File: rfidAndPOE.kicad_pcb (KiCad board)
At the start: 4 copper layers, 100 x 50 mm, 126 parts, among them J1 0813-1X1T-57-F, J2 SWD, J3 MCU Port B, J4 MCU Port C, P1 PoE-, P2 PoE+, P3 GND, P4 +5V, P5 +12V, P6 +3V3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

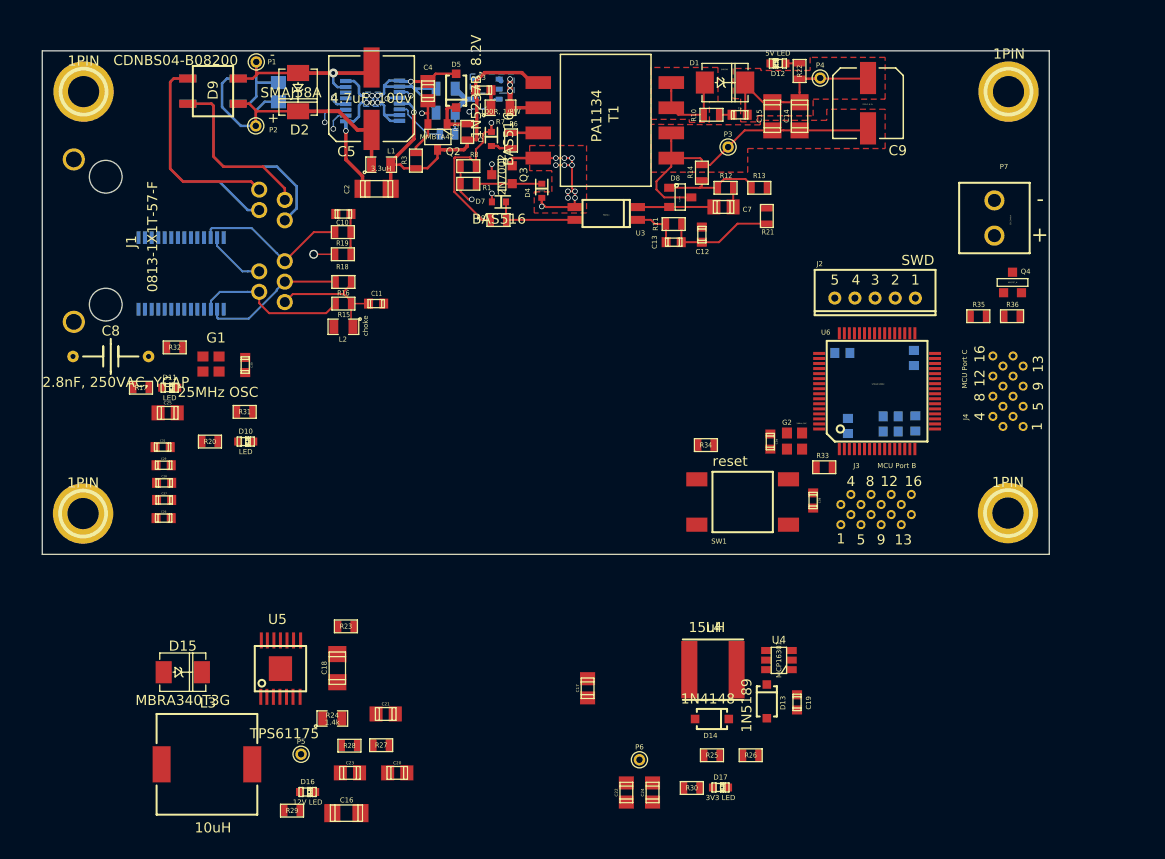
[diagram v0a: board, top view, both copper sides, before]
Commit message: Placed and routed most of the enc28j60 components. Moved TPS61175 (12v boost supply) and components in to good orientation. Almost ready to route. Added ground plane on most of the board.
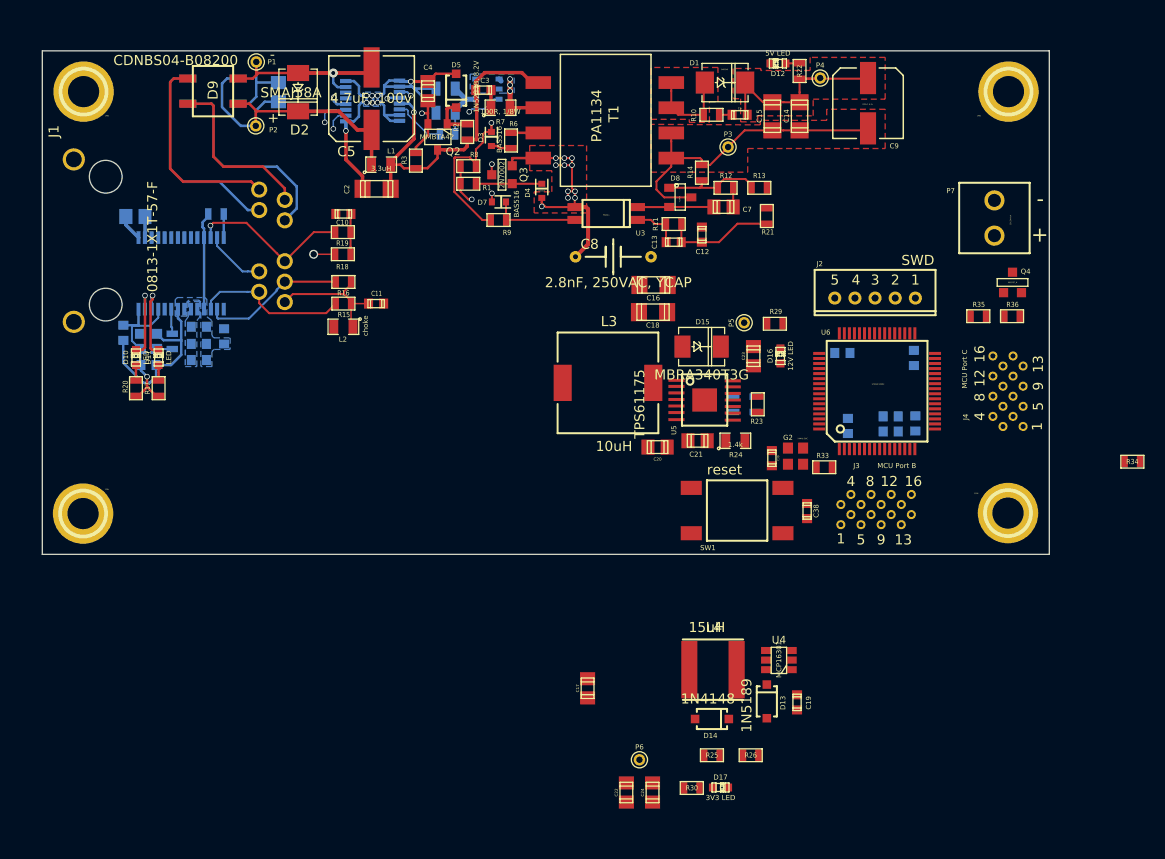
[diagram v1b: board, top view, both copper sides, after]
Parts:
- C25, C26, C27, C28, C29, C30, C31, G1, R27, R28, R31, R32: moved to B.Cu
- moved R29 68.1 mm to (150.6, 57.8)
- moved D16 63.9 mm to (151.1, 61.0), turned to 90 degrees
- moved P5 61.4 mm to (147.5, 57.7), turned to 90 degrees
- moved D15 60.8 mm to (143.3, 60.1)
- moved C16 60.7 mm to (138.5, 54.0), turned to 180 degrees
- moved C23 57.6 mm to (148.4, 61.0), turned to 90 degrees
- moved L3 55.0 mm to (134.0, 63.7)
- moved R28 52.7 mm to (148.6, 65.8), turned to 90 degrees
- moved C8 50.9 mm to (134.5, 51.1)
- moved U5 49.9 mm to (143.6, 65.4), turned to 270 degrees
- moved R27 48.7 mm to (146.4, 65.8), turned to 270 degrees
- moved R24 48.6 mm to (146.6, 69.4)
- moved C18 47.2 mm to (138.4, 56.6), turned to 180 degrees
- moved R23 46.5 mm to (148.8, 65.8), turned to 90 degrees
- moved R34 42.4 mm to (186.1, 71.5)
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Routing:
- net GND: track 31.7 -> 61.5 mm
- net 3V3: track 0.00 -> 16.6 mm, vias 0 -> 1
- net Net-(D11-Pad2): track 0.00 -> 7.59 mm, vias 0 -> 1
- net Net-(D10-Pad2): track 0.00 -> 7.51 mm, vias 0 -> 1
- net GNDA: track 61.2 -> 67.9 mm
- net Net-(C25-Pad2): track 0.00 -> 2.62 mm
- net Net-(R32-Pad2): track 0.00 -> 2.47 mm
- net Net-(R31-Pad2): track 0.00 -> 2.35 mm
- net Net-(G1-Pad3): track 0.00 -> 1.55 mm
- net Net-(D11-Pad1): track 0.00 -> 1.54 mm
- net Net-(D10-Pad1): track 0.00 -> 1.54 mm
- net /TPIN-: track 15.8 -> 16.5 mm, vias 0 -> 1
- added copper zone on B.Cu, net 3V3
- added copper zone on B.Cu, net GND
- added copper zone on In2.Cu, net GND
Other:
- board text added: "Pin 1"

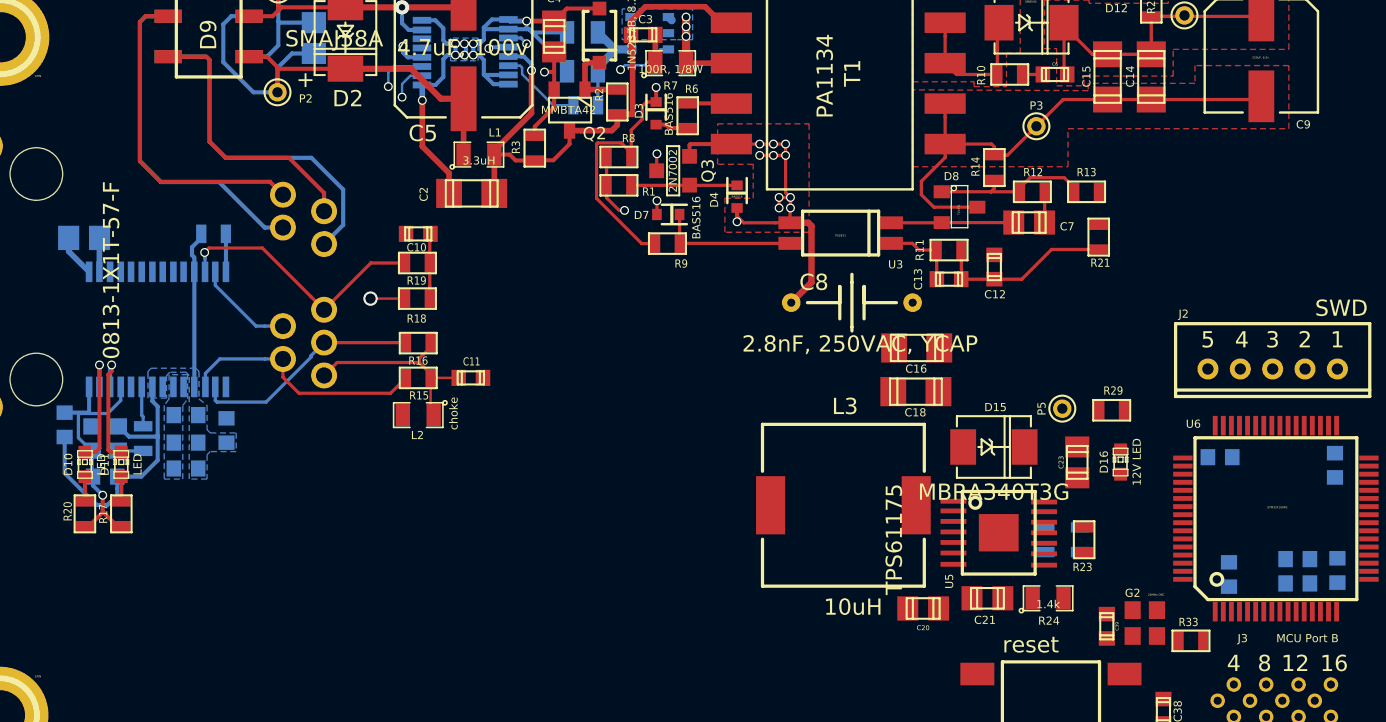
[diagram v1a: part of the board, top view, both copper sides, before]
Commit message: Routed 12V boost supply.
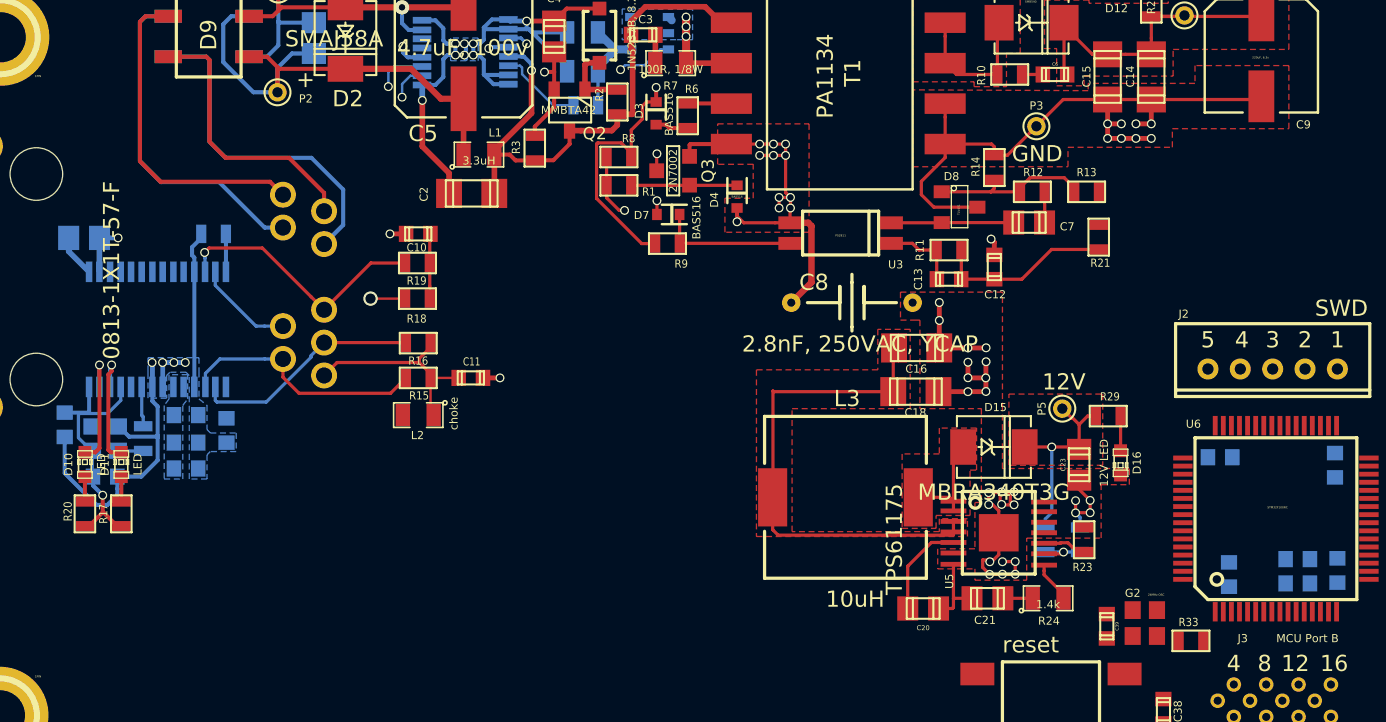
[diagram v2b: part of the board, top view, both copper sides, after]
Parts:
- moved L3 0.51 mm to (134.1, 63.2)
- moved R29 0.42 mm to (150.3, 58.2)
- moved C23 0.19 mm to (148.5, 61.2)
- turned D16 to 270 degrees
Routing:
- net GND: track 61.5 -> 113.8 mm, vias 0 -> 42
- net 5VPoE: track 20.8 -> 51.7 mm
- net 12V: track 0.00 -> 12.8 mm, vias 0 -> 1
- net Net-(D15-Pad1): track 0.00 -> 6.47 mm
- net Net-(C20-Pad1): track 0.00 -> 6.05 mm
- net Net-(R27-Pad2): track 0.00 -> 3.40 mm, vias 0 -> 1
- net Net-(R23-Pad1): track 0.00 -> 2.73 mm
- net Net-(R24-Pad2): track 0.00 -> 2.55 mm
- net Net-(D16-Pad1): track 0.00 -> 2.14 mm
- net Net-(C21-Pad1): track 0.00 -> 1.84 mm
- added copper zone on F.Cu, net 12V
- added copper zone on F.Cu, net Net-(D15-Pad1)
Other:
- board text added: "12V"
- board text added: "GND"

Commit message: Positions the 3.3v supply.
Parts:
- moved D17 55.4 mm to (106.5, 64.1), turned to 90 degrees
- moved R30 50.7 mm to (106.5, 67.9), turned to 90 degrees
- moved C24 50.0 mm to (109.1, 63.9), turned to 270 degrees
- moved C22 47.2 mm to (111.5, 63.8), turned to 270 degrees
- moved D13 46.3 mm to (116.7, 62.8), turned to 180 degrees
- moved R26 44.9 mm to (125.4, 61.9), turned to 180 degrees
- moved C19 43.4 mm to (122.1, 64.7), turned to 0 degrees
- moved P6 42.5 mm to (110.0, 68.3), turned to 180 degrees
- moved U4 41.5 mm to (121.6, 61.9)
- moved R25 41.1 mm to (125.4, 64.1)
- moved C17 37.3 mm to (116.9, 59.8), turned to 0 degrees
- moved L4 37.2 mm to (116.3, 67.8)
- moved D14 37.2 mm to (122.0, 67.2)
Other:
- board text added: "3.3V"

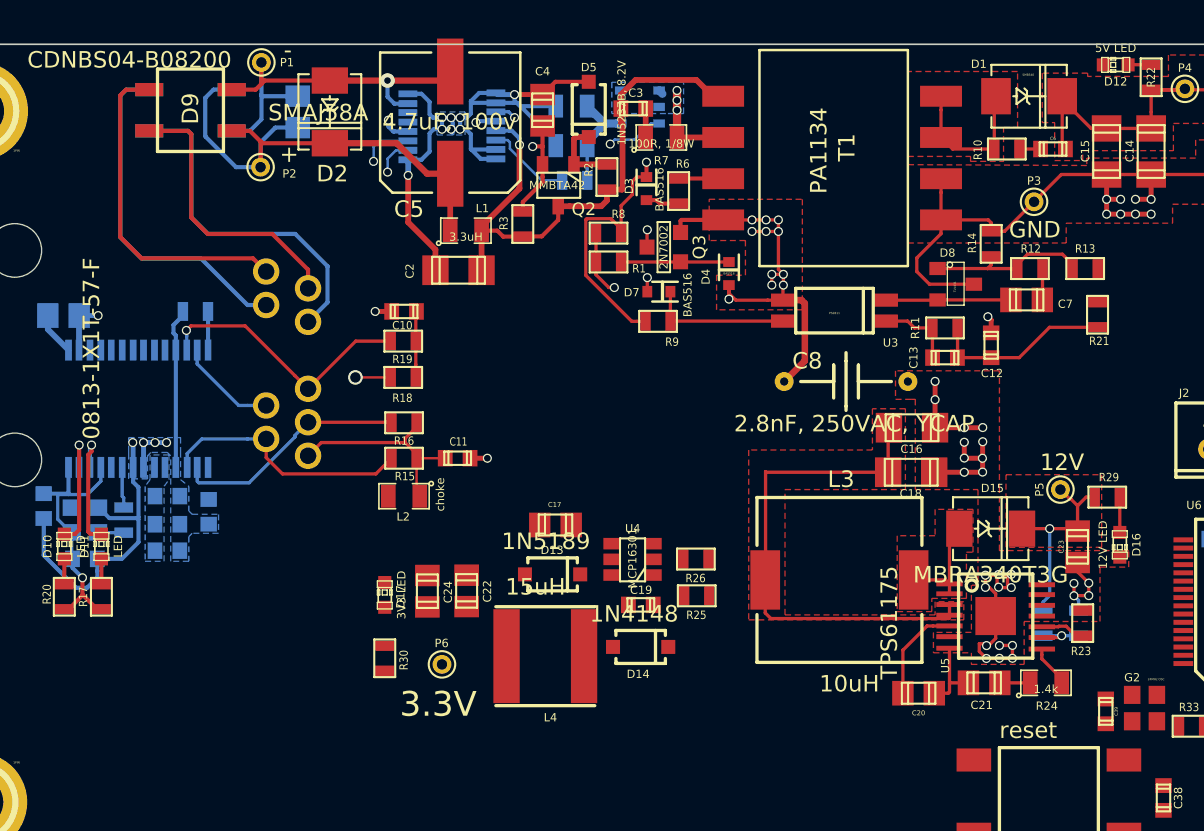
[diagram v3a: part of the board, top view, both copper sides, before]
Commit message: Routed 3.3V supply.
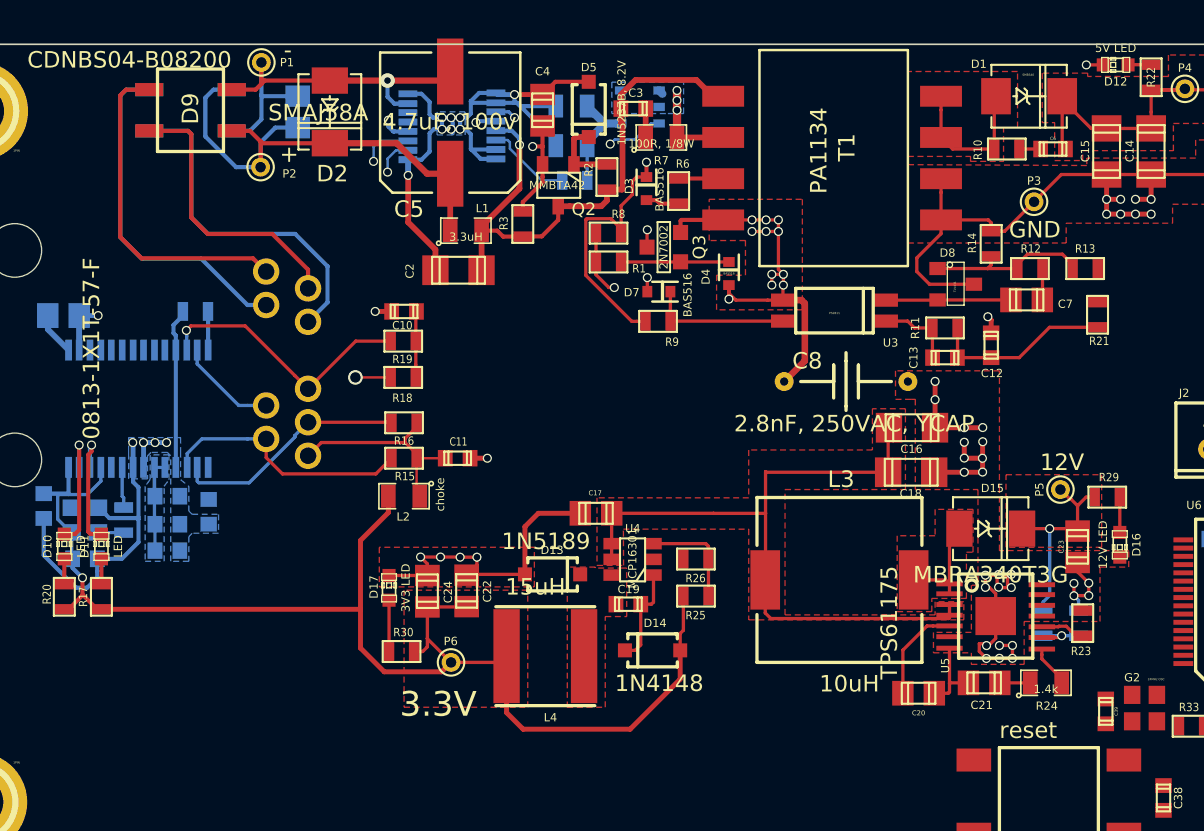
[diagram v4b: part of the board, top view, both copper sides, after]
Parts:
- moved C17 2.56 mm to (119.3, 59.1)
- moved R30 1.10 mm to (107.5, 67.5), turned to 180 degrees
- moved C19 0.76 mm to (121.3, 64.7)
- moved D14 0.75 mm to (122.8, 67.5), turned to 0 degrees
- moved P6 0.56 mm to (110.5, 68.2)
- moved D17 0.50 mm to (106.8, 63.7)
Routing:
- net 3V3: track 16.6 -> 88.1 mm
- net GND: track 113.8 -> 133.3 mm, vias 42 -> 47
- net 5VPoE: track 51.7 -> 63.8 mm
- net Net-(R25-Pad2): track 0.00 -> 6.42 mm
- net Net-(C19-Pad1): track 0.00 -> 6.03 mm
- net Net-(D17-Pad1): track 0.00 -> 3.11 mm
- added copper zone on F.Cu, net 3V3
- added copper zone on F.Cu, net Net-(C19-Pad2)

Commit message: Routed 5V to switch mode supplies and routed 3.3v to ethernet chip.
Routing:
- net 5VPoE: track 63.8 -> 123.2 mm, vias 0 -> 16
- net 3V3: track 88.1 -> 102.5 mm, vias 1 -> 4
- added copper zone on B.Cu, net 5VPoE

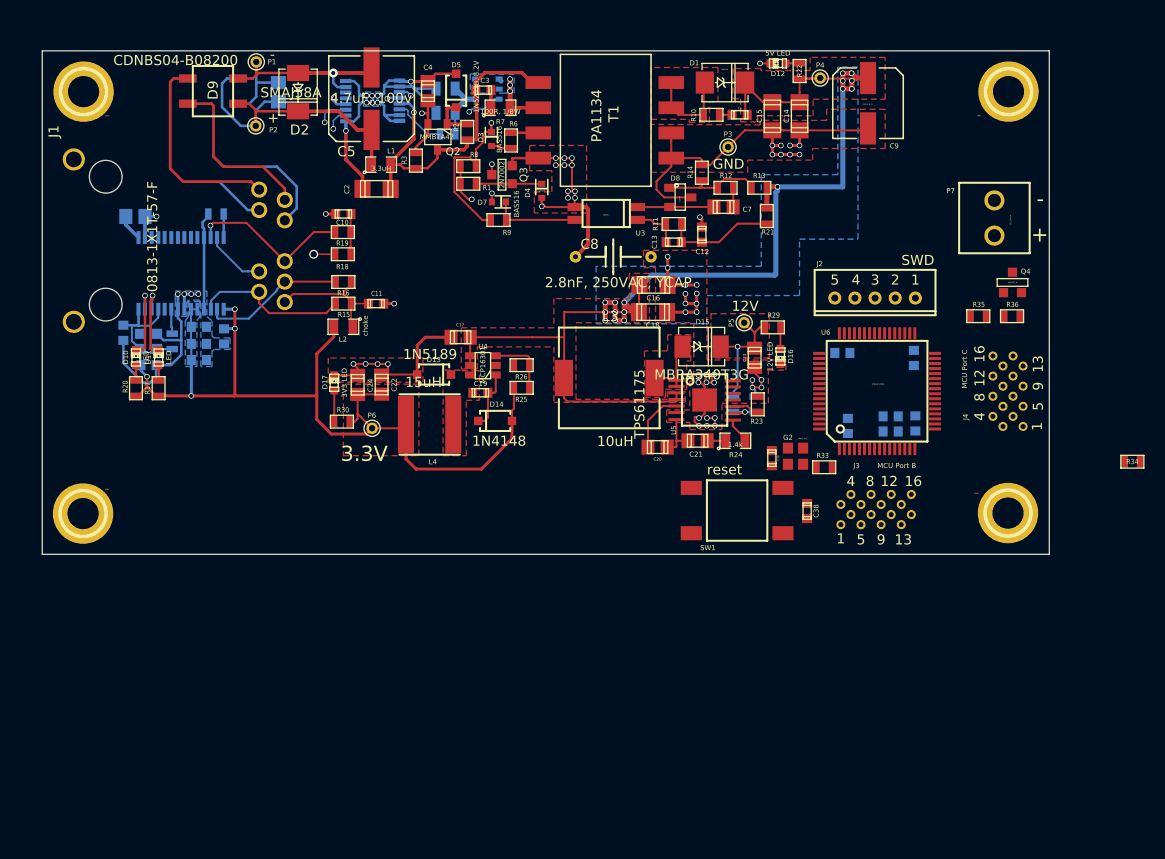
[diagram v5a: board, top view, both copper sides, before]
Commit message: Finished routing microcontroller breakouts and peripherals.
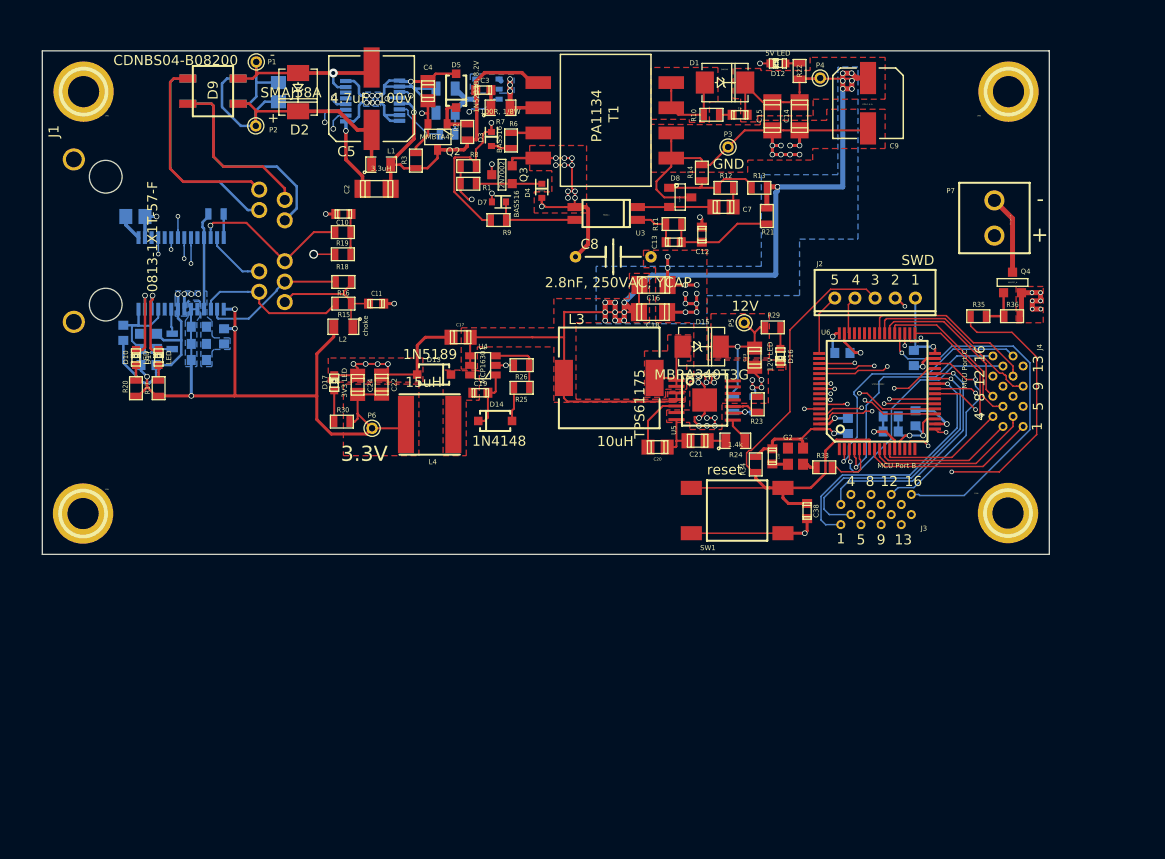
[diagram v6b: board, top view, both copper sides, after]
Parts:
- moved R34 37.4 mm to (148.7, 71.8), turned to 90 degrees
- moved C35 0.51 mm to (164.5, 67.2)
- moved C39 0.19 mm to (150.3, 71.0)
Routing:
- net /EthernetINT: track 0.00 -> 88.5 mm, vias 0 -> 2
- net /EthernetSI: track 0.00 -> 85.5 mm, vias 0 -> 2
- net /EthernetSO: track 0.00 -> 85.1 mm, vias 0 -> 2
- net /EthernetSCK: track 0.00 -> 84.6 mm, vias 0 -> 2
- net /EthernetCS: track 0.00 -> 84.3 mm, vias 0 -> 2
- net /nRST: track 0.00 -> 54.5 mm
- net GND: track 133.3 -> 178.7 mm, vias 47 -> 62
- net /PB15: track 0.00 -> 37.4 mm, vias 0 -> 1
- net /PB10: track 0.00 -> 34.4 mm, vias 0 -> 1
- net /12VSwitch: track 0.00 -> 33.1 mm, vias 0 -> 2
- net /PB12: track 0.00 -> 28.7 mm, vias 0 -> 1
- net /PB1: track 0.00 -> 27.4 mm, vias 0 -> 1
- net /PB0: track 0.00 -> 26.9 mm, vias 0 -> 1
- net /PC13: track 0.00 -> 26.7 mm, vias 0 -> 1
- net /PB13: track 0.00 -> 26.6 mm, vias 0 -> 1
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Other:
- net class Default: clearance 0.2 -> 0.15
- rule trace_clearance: 0.2 -> 0.15
- rule via_min_size: 0.45 -> 0.3
